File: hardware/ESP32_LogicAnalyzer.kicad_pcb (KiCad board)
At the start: 2 copper layers, 48 x 51.8 mm, 12 parts, among them J1 Conn_01x15, J2 Conn_01x15, J5 DEBUG, J6 CHANNELS, U1 SN74LVC245APW, U2 SN74LVC245APW

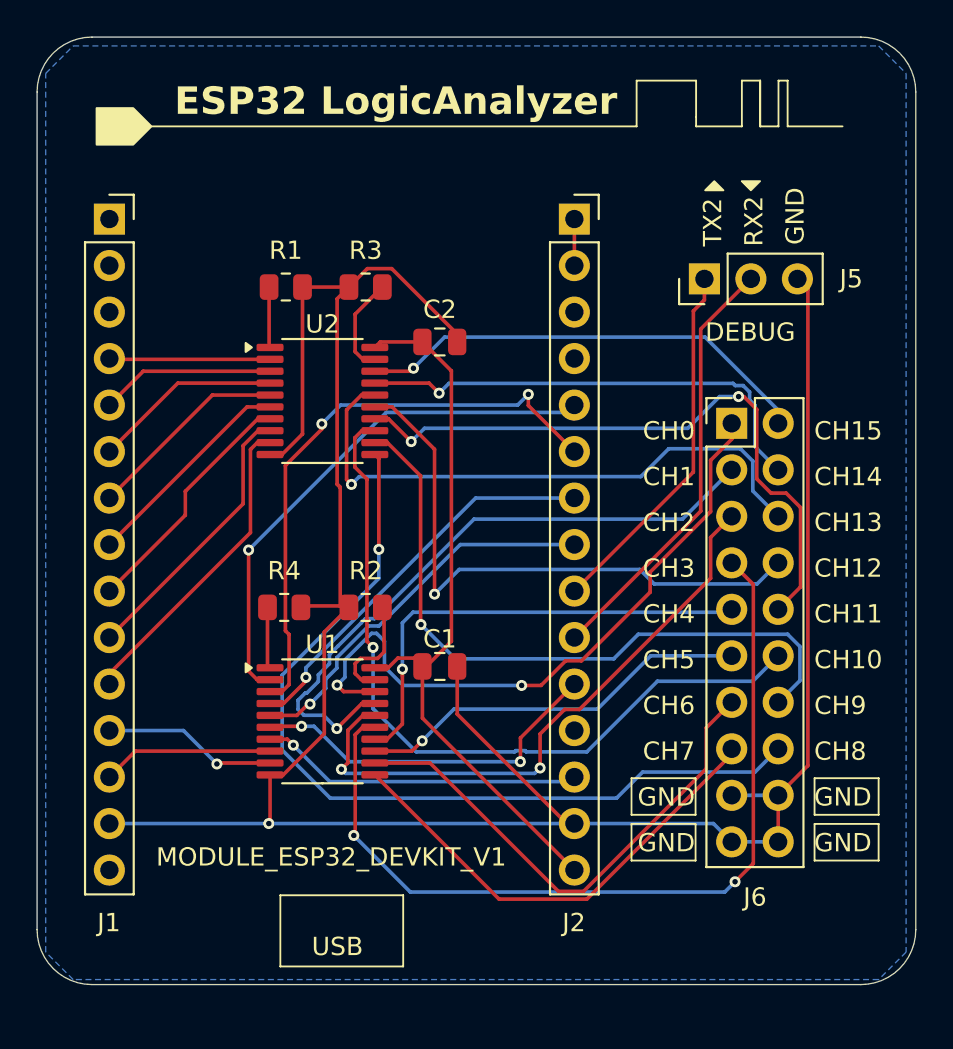
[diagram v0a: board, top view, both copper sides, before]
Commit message: Update ESP32 PCB hardware files
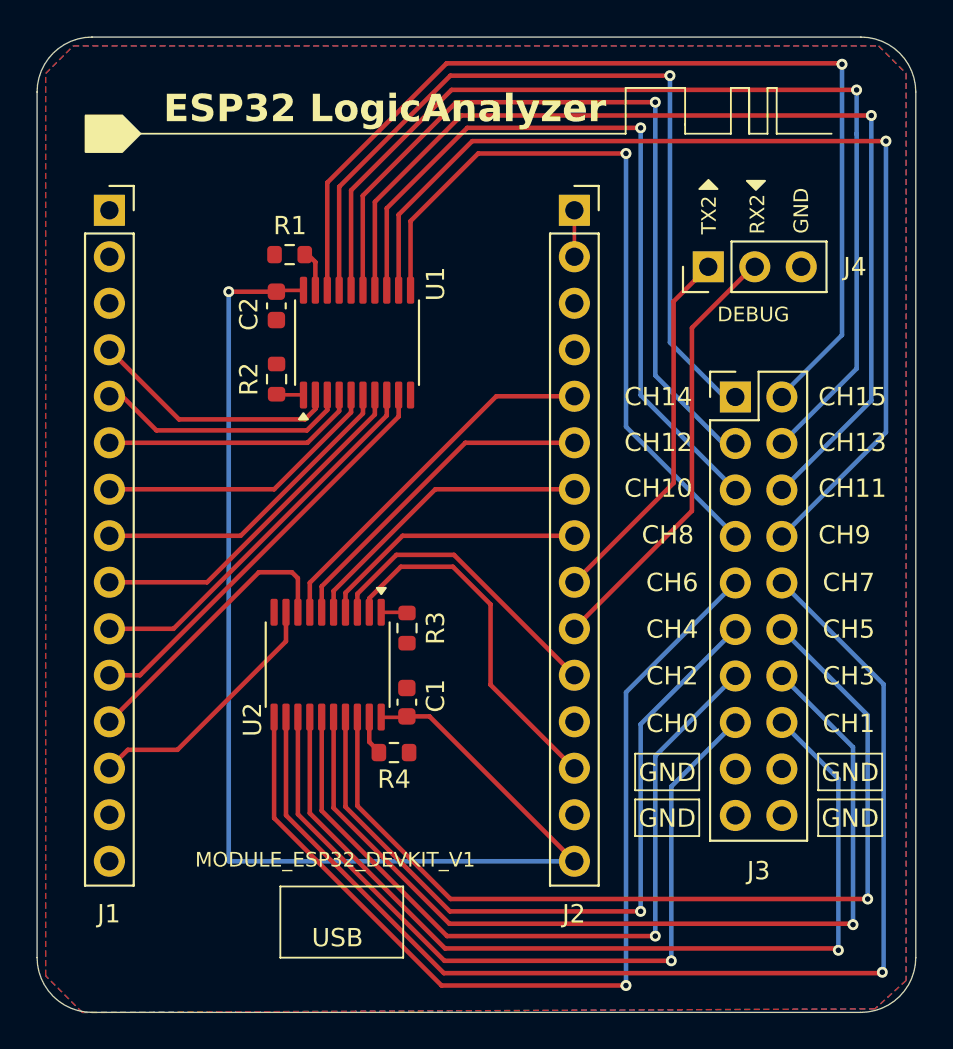
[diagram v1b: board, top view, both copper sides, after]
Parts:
- C1, C2: value 0.1uF -> 100n; footprint Capacitor_SMD:C_0805_2012Metric -> Capacitor_SMD:C_0603_1608Metric
- R1: renamed from R3; footprint Resistor_SMD:R_0805_2012Metric -> Resistor_SMD:R_0603_1608Metric
- R2: renamed from R1; footprint Resistor_SMD:R_0805_2012Metric -> Resistor_SMD:R_0603_1608Metric
- R3: renamed from R4; footprint Resistor_SMD:R_0805_2012Metric -> Resistor_SMD:R_0603_1608Metric
- R4: renamed from R2; footprint Resistor_SMD:R_0805_2012Metric -> Resistor_SMD:R_0603_1608Metric
- moved C2 9.14 mm to (141.1, 84.2), turned to 90 degrees
- moved R4 8.08 mm to (147.5, 108.6), turned to 0 degrees
- moved R3 6.80 mm to (148.2, 101.8), turned to 90 degrees
- moved R2 5.06 mm to (141.1, 88.2), turned to 90 degrees
- moved R1 4.52 mm to (141.8, 81.4)
- moved U1 3.71 mm to (145.5, 86.2), turned to 90 degrees
- moved U2 3.11 mm to (143.9, 103.8), turned to -90 degrees
- moved C1 2.66 mm to (148.2, 105.8), turned to -90 degrees
- moved J3 1.45 mm to (166.2, 89.2)
- moved J4 0.69 mm to (164.7, 82.1)
- moved J1 0.48 mm to (132.0, 79.0)
- moved J2 0.48 mm to (157.4, 79.0)
- renumbered J6 to J3, J5 to J4, U2 to U1, U1 to U2
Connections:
- net /CH15 renamed /CH15_B
- net Net-(J1-Pin_10) renamed /CH9_A
- net Net-(J1-Pin_11) renamed /CH8_A
- net Net-(J1-Pin_4) renamed /CH15_A
- net Net-(J1-Pin_5) renamed /CH14_A
- net Net-(J1-Pin_6) renamed /CH13_A
- net Net-(J1-Pin_7) renamed /CH12_A
- net Net-(J1-Pin_8) renamed /CH11_A
- net Net-(J1-Pin_9) renamed /CH10_A
- J1 pad 12: Net-(J1-Pin_12) -> /CH7_A
- J1 pad 13: Net-(J1-Pin_13) -> /CH6_A
- J2 pad 11: Net-(J2-Pin_11) -> /CH4_A
- J2 pad 13: Net-(J2-Pin_13) -> /CH5_A
- J2 pad 5: Net-(J2-Pin_5) -> /CH0_A
- J2 pad 6: Net-(J2-Pin_6) -> /CH1_A
- J2 pad 7: Net-(J2-Pin_7) -> /CH2_A
- J2 pad 8: Net-(J2-Pin_8) -> /CH3_A
- J3 pad 1: /CH0 -> /CH14_B
- J3 pad 10: /CH11 -> /CH7_B
- J3 pad 11: /CH5 -> /CH4_B
- J3 pad 12: /CH10 -> /CH5_B
- J3 pad 13: /CH6 -> /CH2_B
- J3 pad 14: /CH9 -> /CH3_B
- J3 pad 15: /CH7 -> /CH0_B
- J3 pad 16: /CH8 -> /CH1_B
- J3 pad 3: /CH1 -> /CH12_B
- J3 pad 4: /CH14 -> /CH13_B
- J3 pad 5: /CH2 -> /CH10_B
- J3 pad 6: /CH13 -> /CH11_B
- J3 pad 7: /CH3 -> /CH8_B
- J3 pad 8: /CH12 -> /CH9_B
- J3 pad 9: /CH4 -> /CH6_B
- U1 pad 11: /CH8 -> /CH8_B
- U1 pad 12: /CH9 -> /CH9_B
- U1 pad 13: /CH10 -> /CH10_B
- U1 pad 14: /CH11 -> /CH11_B
- U1 pad 15: /CH12 -> /CH12_B
- U1 pad 16: /CH13 -> /CH13_B
- U1 pad 17: /CH14 -> /CH14_B
- U2 pad 11: /CH7 -> /CH6_B
- U2 pad 12: /CH6 -> /CH7_B
- U2 pad 13: /CH5 -> /CH0_B
- U2 pad 14: /CH4 -> /CH1_B
- U2 pad 15: /CH3 -> /CH2_B
- U2 pad 16: /CH2 -> /CH3_B
- U2 pad 17: /CH1 -> /CH4_B
- U2 pad 18: /CH0 -> /CH5_B
- U2 pad 2: Net-(J2-Pin_5) -> /CH5_A
- U2 pad 3: Net-(J2-Pin_6) -> /CH4_A
- U2 pad 4: Net-(J2-Pin_7) -> /CH3_A
- U2 pad 5: Net-(J2-Pin_8) -> /CH2_A
- U2 pad 6: Net-(J2-Pin_11) -> /CH1_A
- U2 pad 7: Net-(J2-Pin_13) -> /CH0_A
- U2 pad 8: Net-(J1-Pin_13) -> /CH7_A
- U2 pad 9: Net-(J1-Pin_12) -> /CH6_A
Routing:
- net GND: track 138.4 -> 0.00 mm, vias 1 -> 0
- net /CH7_B: track 0.00 -> 65.1 mm, vias 0 -> 1
- net /CH11_B: track 0.00 -> 56.4 mm, vias 0 -> 1
- net /CH9_B: track 0.00 -> 56.4 mm, vias 0 -> 1
- net /CH13_B: track 0.00 -> 56.4 mm, vias 0 -> 1
- net /CH6_B: track 0.00 -> 53.0 mm, vias 0 -> 1
- net /CH5_B: track 0.00 -> 51.5 mm, vias 0 -> 1
- net /CH3_B: track 0.00 -> 51.2 mm, vias 0 -> 1
- net /CH1_B: track 0.00 -> 50.9 mm, vias 0 -> 1
- net /CH8: track 47.7 -> 0.00 mm, vias 1 -> 0
- net /CH3: track 47.4 -> 0.00 mm, vias 2 -> 0
- net /CH14_B: track 0.00 -> 45.6 mm, vias 0 -> 1
- net /CH12_B: track 0.00 -> 44.4 mm, vias 0 -> 1
- net /CH0_B: track 0.00 -> 43.5 mm, vias 0 -> 1
- net /CH2_B: track 0.00 -> 42.2 mm, vias 0 -> 1
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- added copper zone on F.Cu, net GND
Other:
- board size 48 x 51.8 mm -> 48 x 53.3 mm
